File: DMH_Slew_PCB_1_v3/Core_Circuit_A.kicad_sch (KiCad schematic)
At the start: 60 parts, among them J1 TS_Jack_6.35mm_Sw, J11 Conn_02x03_Top_Bottom, J12 Conn_02x06_Top_Bottom, J13 Conn_02x03_Top_Bottom, J14 Conn_02x03_Top_Bottom, J15 Conn_02x06_Top_Bottom, J16 Conn_02x03_Top_Bottom, J17 Conn_01x08, J18 Conn_01x08, J19 Conn_01x08, J2 TS_Jack_6.35mm_Sw, J20 Conn_01x08, J3 TS_Jack_6.35mm_Sw, Q1 BC548, Q2 BC548, Q3 BC558, Q4 BC558, SW1 SW_DPDT_3way, SW2 SW_DPDT, SW3 SPDT_OnOffOn, U1 TL074, U2 TL074

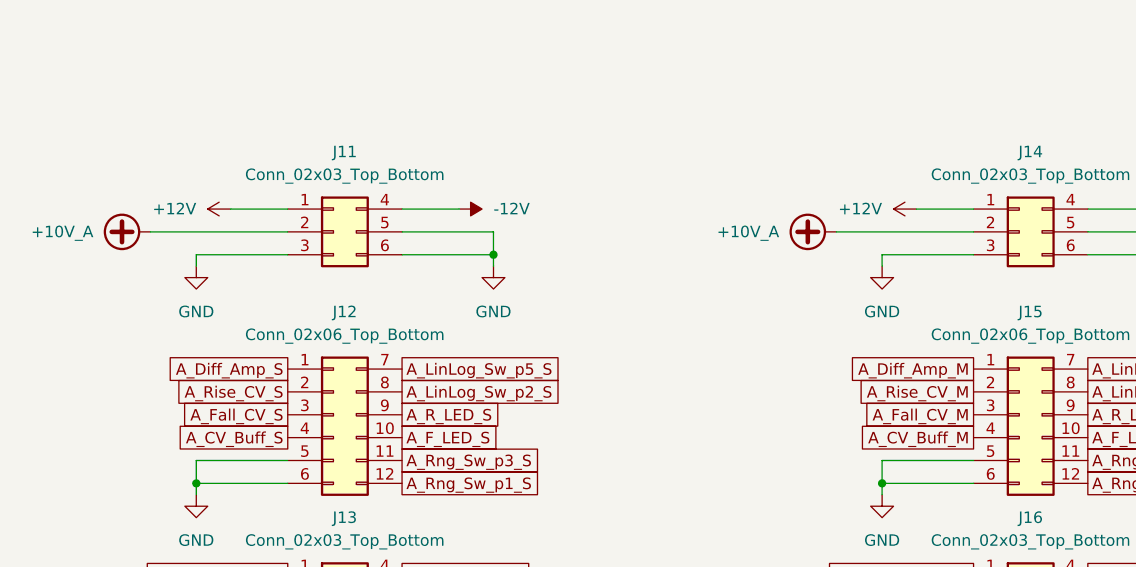
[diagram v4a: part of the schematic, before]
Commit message: PCB 1 routing in progress
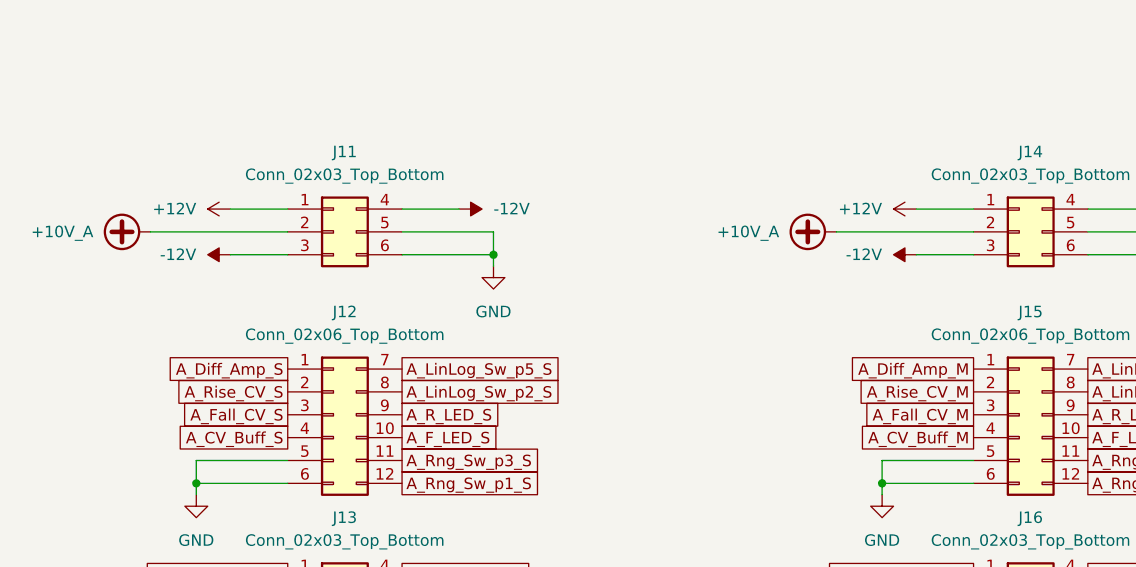
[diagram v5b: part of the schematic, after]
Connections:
- net -12V: now also J11.3 (Pin_3), J14.3 (Pin_3)
- net GND: no longer J11.3 (Pin_3), J14.3 (Pin_3)
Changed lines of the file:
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@@
 	(wire
 		(pts
-			(xy 34.29 231.14) (xy 44.45 231.14)
+			(xy 38.1 231.14) (xy 44.45 231.14)
 		)
 		(stroke
@@
 	(wire
 		(pts
-			(xy 120.65 231.14) (xy 110.49 231.14)
-		)
-		(stroke
-			(width 0)
-			(type default)
-		)
-	)
-	(wire
-		(pts
 			(xy 384.81 80.01) (xy 387.35 80.01)
 		)
@@
 	(wire
 		(pts
-			(xy 34.29 232.41) (xy 34.29 231.14)
-		)
-		(stroke
-			(width 0)
-			(type default)
-		)
-	)
-	(wire
-		(pts
 			(xy 191.77 158.75) (xy 191.77 165.1)
 		)
@@
 	(wire
 		(pts
-			(xy 200.66 106.68) (xy 203.2 106.68)
+			(xy 114.3 231.14) (xy 120.65 231.14)
 		)
 		(stroke
@@
 	(wire
 		(pts
-			(xy 240.03 182.88) (xy 240.03 171.45)
+			(xy 200.66 106.68) (xy 203.2 106.68)
 		)
 		(stroke
@@
 	(wire
 		(pts
-			(xy 137.16 80.01) (xy 133.35 80.01)
+			(xy 240.03 182.88) (xy 240.03 171.45)
 		)
 		(stroke
@@
 	(wire
 		(pts
-			(xy 266.7 83.82) (xy 271.78 83.82)
+			(xy 137.16 80.01) (xy 133.35 80.01)
 		)
 		(stroke
@@
 	(wire
 		(pts
-			(xy 215.9 139.7) (xy 215.9 142.24)
+			(xy 266.7 83.82) (xy 271.78 83.82)
 		)
 		(stroke
@@
 	(wire
 		(pts
-			(xy 250.19 123.19) (xy 250.19 135.89)
+			(xy 215.9 139.7) (xy 215.9 142.24)
 		)
 		(stroke
@@
 	(wire
 		(pts
-			(xy 228.6 130.81) (xy 228.6 133.35)
+			(xy 250.19 123.19) (xy 250.19 135.89)
 		)
 		(stroke
@@
 	(wire
 		(pts
-			(xy 55.88 165.1) (xy 82.55 165.1)
+			(xy 228.6 130.81) (xy 228.6 133.35)
 		)
 		(stroke
@@
 	(wire
 		(pts
-			(xy 110.49 231.14) (xy 110.49 232.41)
+			(xy 55.88 165.1) (xy 82.55 165.1)
 		)
 		(stroke
@@
 	)
 	(symbol
-		(lib_id "power:GND")
-		(at 110.49 232.41 0)
-		(unit 1)
-		(exclude_from_sim no)
-		(in_bom yes)
-		(on_board yes)
-		(dnp no)
-		(fields_autoplaced yes)
-		(property "Reference" "#PWR091"
-			(at 110.49 238.76 0)
-			(effects
-				(font
-					(size 1.27 1.27)
-				)
-				(hide yes)
-			)
-		)
-		(property "Value" "GND"
-			(at 110.49 237.49 0)
-			(effects
-				(font
-					(size 1.27 1.27)
-				)
-			)
-		)
-		(property "Footprint" ""
-			(at 110.49 232.41 0)
-			(effects
-				(font
-					(size 1.27 1.27)
-				)
-				(hide yes)
-			)
-		)
-		(property "Datasheet" ""
-			(at 110.49 232.41 0)
-			(effects
-				(font
-					(size 1.27 1.27)
-				)
-				(hide yes)
-			)
-		)
-		(property "Description" "Power symbol creates a global label with name \"GND\" , ground"
-			(at 110.49 232.41 0)
-			(effects
-				(font
-					(size 1.27 1.27)
-				)
-				(hide yes)
-			)
-		)
-		(pin "1"
-		)
-		(instances
-			(project "DMH_Slew_PCB_1_v3"
-				(path "/58f4306d-5387-4983-bb08-41a2313fd315/7ad2d702-dfb7-4d49-a82d-34430dd5948f"
-					(reference "#PWR091")
-					(unit 1)
-				)
-			)
-		)
-	)
-	(symbol
 		(lib_id "Transistor_BJT:BC558")
 		(at 228.6 173.99 270)
@@
 	)
 	(symbol
+		(lib_id "power:-12V")
+		(at 38.1 231.14 90)
+		(unit 1)
+		(exclude_from_sim no)
+		(in_bom yes)
+		(on_board no)
+		(dnp no)
+		(fields_autoplaced yes)
+		(property "Reference" "#PWR087"
+			(at 41.91 231.14 0)
+			(effects
+				(font
+					(size 1.27 1.27)
+				)
+				(hide yes)
+			)
+		)
+		(property "Value" "-12V"
+			(at 34.29 231.1399 90)
+			(effects
+				(font
+					(size 1.27 1.27)
+				)
+				(justify left)
+			)
+		)
+		(property "Footprint" ""
+			(at 38.1 231.14 0)
+			(effects
+				(font
+					(size 1.27 1.27)
+				)
+				(hide yes)
+			)
+		)
+		(property "Datasheet" ""
+			(at 38.1 231.14 0)
+			(effects
+				(font
+					(size 1.27 1.27)
+				)
+				(hide yes)
+			)
+		)
+		(property "Description" "Power symbol creates a global label with name \"-12V\""
+			(at 38.1 231.14 0)
+			(effects
+				(font
+					(size 1.27 1.27)
+				)
+				(hide yes)
+			)
+		)
+		(pin "1"
+		)
+		(instances
+			(project "DMH_Slew_PCB_1_v3"
+				(path "/58f4306d-5387-4983-bb08-41a2313fd315/7ad2d702-dfb7-4d49-a82d-34430dd5948f"
+					(reference "#PWR087")
+					(unit 1)
+				)
+			)
+		)
+	)
+	(symbol
 		(lib_id "power:GND")
 		(at 182.88 251.46 0)
@@
 	(symbol
 		(lib_id "power:GND")
-		(at 34.29 232.41 0)
-		(mirror y)
+		(at 67.31 232.41 0)
 		(unit 1)
 		(exclude_from_sim no)
@@
 		(dnp no)
 		(fields_autoplaced yes)
-		(property "Reference" "#PWR087"
-			(at 34.29 238.76 0)
+		(property "Reference" "#PWR083"
+			(at 67.31 238.76 0)
 			(effects
 				(font
@@
 		)
 		(property "Value" "GND"
-			(at 34.29 237.49 0)
+			(at 67.31 237.49 0)
 			(effects
 				(font
@@
 		)
 		(property "Footprint" ""
-			(at 34.29 232.41 0)
+			(at 67.31 232.41 0)
 			(effects
 				(font
@@
 		)
 		(property "Datasheet" ""
-			(at 34.29 232.41 0)
+			(at 67.31 232.41 0)
 			(effects
 				(font
@@
 		)
 		(property "Description" "Power symbol creates a global label with name \"GND\" , ground"
-			(at 34.29 232.41 0)
+			(at 67.31 232.41 0)
 			(effects
 				(font
@@
 		)
 		(instances
-			(project "DMH_Slew_PCB_1_v3"
+			(project ""
 				(path "/58f4306d-5387-4983-bb08-41a2313fd315/7ad2d702-dfb7-4d49-a82d-34430dd5948f"
-					(reference "#PWR087")
+					(reference "#PWR083")
 					(unit 1)
 				)
@@
 	)
 	(symbol
-		(lib_id "power:GND")
-		(at 67.31 232.41 0)
+		(lib_id "power:-12V")
+		(at 114.3 231.14 90)
 		(unit 1)
 		(exclude_from_sim no)
 		(in_bom yes)
-		(on_board no)
+		(on_board yes)
 		(dnp no)
 		(fields_autoplaced yes)
-		(property "Reference" "#PWR083"
-			(at 67.31 238.76 0)
+		(property "Reference" "#PWR091"
+			(at 118.11 231.14 0)
 			(effects
 				(font
@@
 			)
 		)
-		(property "Value" "GND"
-			(at 67.31 237.49 0)
+		(property "Value" "-12V"
+			(at 110.49 231.1399 90)
 			(effects
 				(font
 					(size 1.27 1.27)
 				)
+				(justify left)
 			)
 		)
 		(property "Footprint" ""
-			(at 67.31 232.41 0)
+			(at 114.3 231.14 0)
 			(effects
 				(font
@@
 		)
 		(property "Datasheet" ""
-			(at 67.31 232.41 0)
+			(at 114.3 231.14 0)
 			(effects
 				(font
@@
 			)
 		)
-		(property "Description" "Power symbol creates a global label with name \"GND\" , ground"
-			(at 67.31 232.41 0)
+		(property "Description" "Power symbol creates a global label with name \"-12V\""
+			(at 114.3 231.14 0)
 			(effects
 				(font
@@
 		)
 		(instances
-			(project ""
+			(project "DMH_Slew_PCB_1_v3"
 				(path "/58f4306d-5387-4983-bb08-41a2313fd315/7ad2d702-dfb7-4d49-a82d-34430dd5948f"
-					(reference "#PWR083")
+					(reference "#PWR091")
 					(unit 1)
 				)

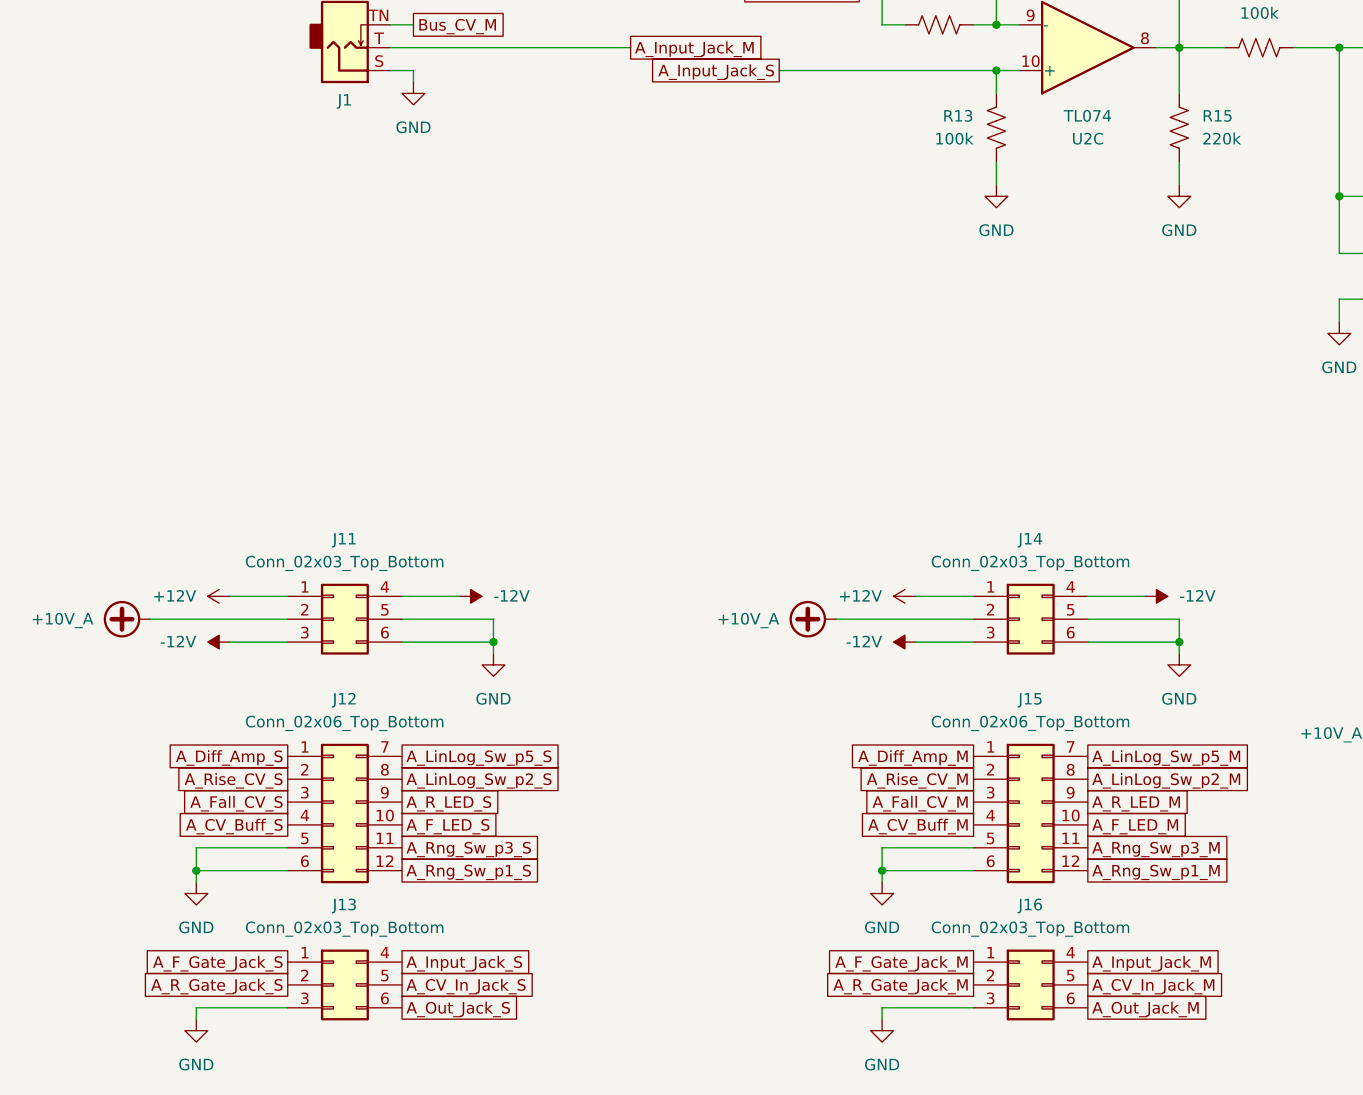
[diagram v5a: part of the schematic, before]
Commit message: Exposed loopback resistor to submodule connector
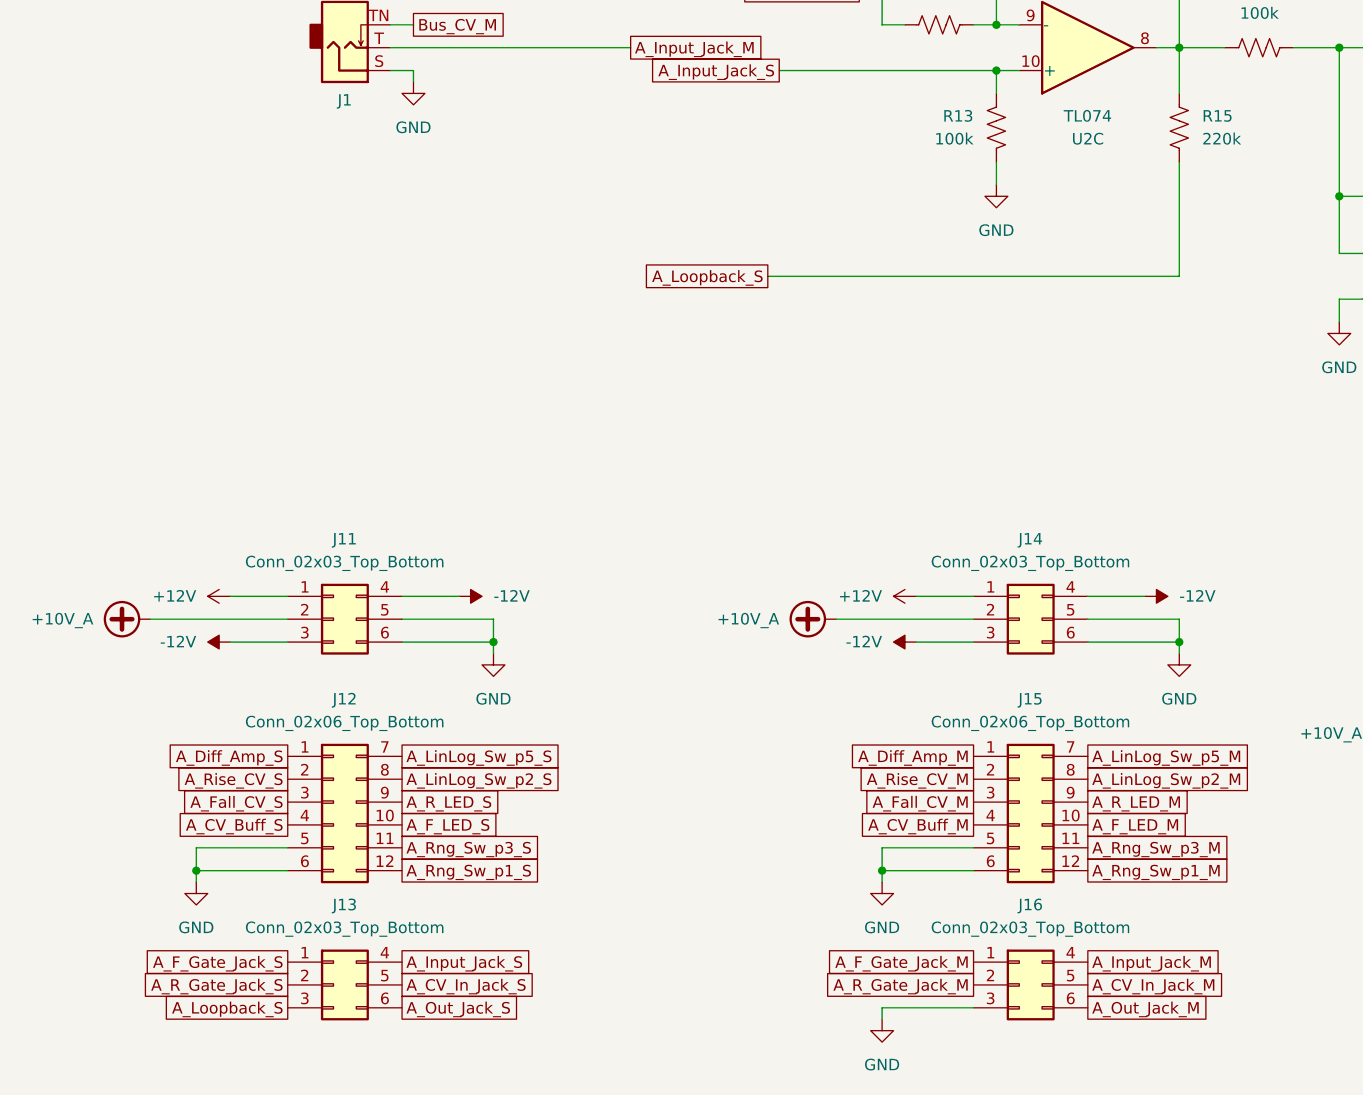
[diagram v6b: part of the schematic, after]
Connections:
- net GND: no longer J13.3 (Pin_3), R15.2
- new net A_Loopback_S: J13.3 (Pin_3), R15.2
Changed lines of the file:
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@@
 	(wire
 		(pts
-			(xy 110.49 271.78) (xy 110.49 273.05)
-		)
-		(stroke
-			(width 0)
-			(type default)
-		)
-	)
-	(wire
-		(pts
 			(xy 154.94 91.44) (xy 163.83 91.44)
 		)
@@
 	(wire
 		(pts
-			(xy 143.51 177.8) (xy 143.51 180.34)
+			(xy 143.51 177.8) (xy 143.51 190.5)
 		)
 		(stroke
@@
 	(wire
 		(pts
-			(xy 44.45 271.78) (xy 34.29 271.78)
-		)
-		(stroke
-			(width 0)
-			(type default)
-		)
-	)
-	(wire
-		(pts
 			(xy 167.64 104.14) (xy 167.64 97.79)
 		)
@@
 	(wire
 		(pts
-			(xy 120.65 271.78) (xy 110.49 271.78)
-		)
-		(stroke
-			(width 0)
-			(type default)
-		)
-	)
-	(wire
-		(pts
 			(xy 322.58 132.08) (xy 323.85 132.08)
 		)
@@
 	(wire
 		(pts
+			(xy 120.65 271.78) (xy 110.49 271.78)
+		)
+		(stroke
+			(width 0)
+			(type default)
+		)
+	)
+	(wire
+		(pts
 			(xy 29.21 228.6) (xy 44.45 228.6)
 		)
@@
 	(wire
 		(pts
-			(xy 34.29 271.78) (xy 34.29 273.05)
+			(xy 97.79 190.5) (xy 143.51 190.5)
 		)
 		(stroke
@@
 	(wire
 		(pts
+			(xy 110.49 271.78) (xy 110.49 273.05)
+		)
+		(stroke
+			(width 0)
+			(type default)
+		)
+	)
+	(wire
+		(pts
 			(xy 384.81 68.58) (xy 393.7 68.58)
 		)
@@
 		)
 	)
+	(global_label "A_Loopback_S"
+		(shape passive)
+		(at 44.45 271.78 180)
+		(fields_autoplaced yes)
+		(effects
+			(font
+				(size 1.27 1.27)
+			)
+			(justify right)
+		)
+		(property "Intersheetrefs" "${INTERSHEET_REFS}"
+			(at 29.453 271.78 0)
+			(effects
+				(font
+					(size 1.27 1.27)
+				)
+				(justify right)
+				(hide yes)
+			)
+		)
+	)
 	(global_label "A_Rise_CV_S"
 		(shape passive)
@@
 		)
 	)
+	(global_label "A_Loopback_S"
+		(shape passive)
+		(at 97.79 190.5 180)
+		(fields_autoplaced yes)
+		(effects
+			(font
+				(size 1.27 1.27)
+			)
+			(justify right)
+		)
+		(property "Intersheetrefs" "${INTERSHEET_REFS}"
+			(at 82.793 190.5 0)
+			(effects
+				(font
+					(size 1.27 1.27)
+				)
+				(justify right)
+				(hide yes)
+			)
+		)
+	)
 	(global_label "A_Rng_Sw_p3_S"
 		(shape passive)
@@
 		(polyline
 			(pts
-				(xy 44.45 152.4) (xy 78.74 152.4) (xy 78.74 177.8) (xy 44.45 177.8)
+				(xy 45.085 152.4) (xy 79.375 152.4) (xy 79.375 198.12) (xy 45.085 198.12)
 			)
 			(stroke
@@
 		(length 2.54)
 		(shape round)
-		(at 44.45 152.4 0)
+		(at 45.72 152.4 0)
 		(fields_autoplaced yes)
 		(effects
@@
 		)
 		(property "Component Class" "Main PCB"
-			(at 45.1485 149.86 0)
+			(at 46.4185 149.86 0)
 			(effects
 				(font
@@
 	(symbol
 		(lib_id "power:GND")
-		(at 143.51 180.34 0)
-		(unit 1)
-		(exclude_from_sim no)
-		(in_bom yes)
-		(on_board no)
-		(dnp no)
-		(fields_autoplaced yes)
-		(property "Reference" "#PWR022"
-			(at 143.51 186.69 0)
-			(effects
-				(font
-					(size 1.27 1.27)
-				)
-				(hide yes)
-			)
-		)
-		(property "Value" "GND"
-			(at 143.51 185.42 0)
-			(effects
-				(font
-					(size 1.27 1.27)
-				)
-			)
-		)
-		(property "Footprint" ""
-			(at 143.51 180.34 0)
-			(effects
-				(font
-					(size 1.27 1.27)
-				)
-				(hide yes)
-			)
-		)
-		(property "Datasheet" ""
-			(at 143.51 180.34 0)
-			(effects
-				(font
-					(size 1.27 1.27)
-				)
-				(hide yes)
-			)
-		)
-		(property "Description" "Power symbol creates a global label with name \"GND\" , ground"
-			(at 143.51 180.34 0)
-			(effects
-				(font
-					(size 1.27 1.27)
-				)
-				(hide yes)
-			)
-		)
-		(pin "1"
-		)
-		(instances
-			(project "DMH_Slew_PCB_1_v3"
-				(path "/58f4306d-5387-4983-bb08-41a2313fd315/7ad2d702-dfb7-4d49-a82d-34430dd5948f"
-					(reference "#PWR022")
-					(unit 1)
-				)
-			)
-		)
-	)
-	(symbol
-		(lib_id "power:GND")
 		(at 44.45 86.36 0)
 		(unit 1)
@@
 	(symbol
 		(lib_id "power:GND")
-		(at 34.29 273.05 0)
-		(mirror y)
-		(unit 1)
-		(exclude_from_sim no)
-		(in_bom yes)
-		(on_board no)
-		(dnp no)
-		(fields_autoplaced yes)
-		(property "Reference" "#PWR0101"
-			(at 34.29 279.4 0)
-			(effects
-				(font
-					(size 1.27 1.27)
-				)
-				(hide yes)
-			)
-		)
-		(property "Value" "GND"
-			(at 34.29 278.13 0)
-			(effects
-				(font
-					(size 1.27 1.27)
-				)
-			)
-		)
-		(property "Footprint" ""
-			(at 34.29 273.05 0)
-			(effects
-				(font
-					(size 1.27 1.27)
-				)
-				(hide yes)
-			)
-		)
-		(property "Datasheet" ""
-			(at 34.29 273.05 0)
-			(effects
-				(font
-					(size 1.27 1.27)
-				)
-				(hide yes)
-			)
-		)
-		(property "Description" "Power symbol creates a global label with name \"GND\" , ground"
-			(at 34.29 273.05 0)
-			(effects
-				(font
-					(size 1.27 1.27)
-				)
-				(hide yes)
-			)
-		)
-		(pin "1"
-		)
-		(instances
-			(project "DMH_Slew_PCB_1_v3"
-				(path "/58f4306d-5387-4983-bb08-41a2313fd315/7ad2d702-dfb7-4d49-a82d-34430dd5948f"
-					(reference "#PWR0101")
-					(unit 1)
-				)
-			)
-		)
-	)
-	(symbol
-		(lib_id "power:GND")
 		(at 349.25 215.9 0)
 		(unit 1)
@@
 	)
 	(symbol
+		(lib_id "power:GND")
+		(at 110.49 273.05 0)
+		(unit 1)
+		(exclude_from_sim no)
+		(in_bom yes)
+		(on_board yes)
+		(dnp no)
+		(fields_autoplaced yes)
+		(property "Reference" "#PWR022"
+			(at 110.49 279.4 0)
+			(effects
+				(font
+					(size 1.27 1.27)
+				)
+				(hide yes)
+			)
+		)
+		(property "Value" "GND"
+			(at 110.49 278.13 0)
+			(effects
+				(font
+					(size 1.27 1.27)
+				)
+			)
+		)
+		(property "Footprint" ""
+			(at 110.49 273.05 0)
+			(effects
+				(font
+					(size 1.27 1.27)
+				)
+				(hide yes)
+			)
+		)
+		(property "Datasheet" ""
+			(at 110.49 273.05 0)
+			(effects
+				(font
+					(size 1.27 1.27)
+				)
+				(hide yes)
+			)
+		)
+		(property "Description" "Power symbol creates a global label with name \"GND\" , ground"
+			(at 110.49 273.05 0)
+			(effects
+				(font
+					(size 1.27 1.27)
+				)
+				(hide yes)
+			)
+		)
+		(pin "1"
+		)
+		(instances
+			(project ""
+				(path "/58f4306d-5387-4983-bb08-41a2313fd315/7ad2d702-dfb7-4d49-a82d-34430dd5948f"
+					(reference "#PWR022")
+					(unit 1)
+				)
+			)
+		)
+	)
+	(symbol
 		(lib_id "SynthStuff:TS_Jack_6.35mm_Sw")
 		(at 355.6 127 180)
@@
 					(unit 1)
 				)
-			)
-		)
-	)
-	(symbol
-		(lib_id "power:GND")
-		(at 110.49 273.05 0)
-		(mirror y)
-		(unit 1)
-		(exclude_from_sim no)
-		(in_bom yes)
-		(on_board yes)
-		(dnp no)
-		(fields_autoplaced yes)
-		(property "Reference" "#PWR0102"
-			(at 110.49 279.4 0)
-			(effects
-				(font
-					(size 1.27 1.27)
-				)
-				(hide yes)
-			)
-		)
-		(property "Value" "GND"
-			(at 110.49 278.13 0)
-			(effects
-				(font
-					(size 1.27 1.27)
-				)
-			)
-		)
-		(property "Footprint" ""
-			(at 110.49 273.05 0)
-			(effects
-				(font
-					(size 1.27 1.27)
-				)
-				(hide yes)
-			)
-		)
-		(property "Datasheet" ""
-			(at 110.49 273.05 0)
-			(effects
-				(font
-					(size 1.27 1.27)
-				)
-				(hide yes)
-			)
-		)
-		(property "Description" "Power symbol creates a global label with name \"GND\" , ground"
-			(at 110.49 273.05 0)
-			(effects
-				(font
-					(size 1.27 1.27)
-				)
-				(hide yes)
-			)
-		)
-		(pin "1"
-		)
-		(instances
-			(project "DMH_Slew_PCB_1_v3"
-				(path "/58f4306d-5387-4983-bb08-41a2313fd315/7ad2d702-dfb7-4d49-a82d-34430dd5948f"
-					(reference "#PWR0102")
-					(unit 1)
-				)
